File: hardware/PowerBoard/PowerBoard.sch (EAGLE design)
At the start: 137 parts, among them J1 CON-HRS-DM3AT, J2 CON-ZX62R-B-5P, J3 CON-FTSH-105-01-L-DV-K, J4 CON-S2B-PH-SM4-TB, J5 CON-PJ-102A, J6 CON-71741-0002-TOP, M1 MOUNT-HOLE3.3, M2 MOUNT-HOLE3.3, M3 MOUNT-HOLE3.3, M4 MOUNT-HOLE3.3, M5 FIDUCIAL1X2, M6 FIDUCIAL1X2, M7 FIDUCIAL1X2, M8 FIDUCIAL1X2, Q1 SI2323CDS, Q2 SI2312CDS, Q3 SI2333CDS, Q4 SI2333CDS, SW1 SWITCH-SPST, SW2 SWITCH-MS12ASG30, U1 LTC4361-2DC, U10 MAX9938FEUK, U11 MAX9938FEUK, U12 MAX9938FEUK, U13 STM32F10XCXT6, U14 LTC2942-1, U15 USBLC6-2, U2 LTC4085, U3 XC6220B331MR-G, U4 XC6220B331MR-G, U5 XC9236A15DMR-G, U6 MIC94043, U7 MAX9938FEUK, U8 MAX9938FEUK, U9 MAX9938FEUK, X1 ECX-2236, X2 ECX-31B

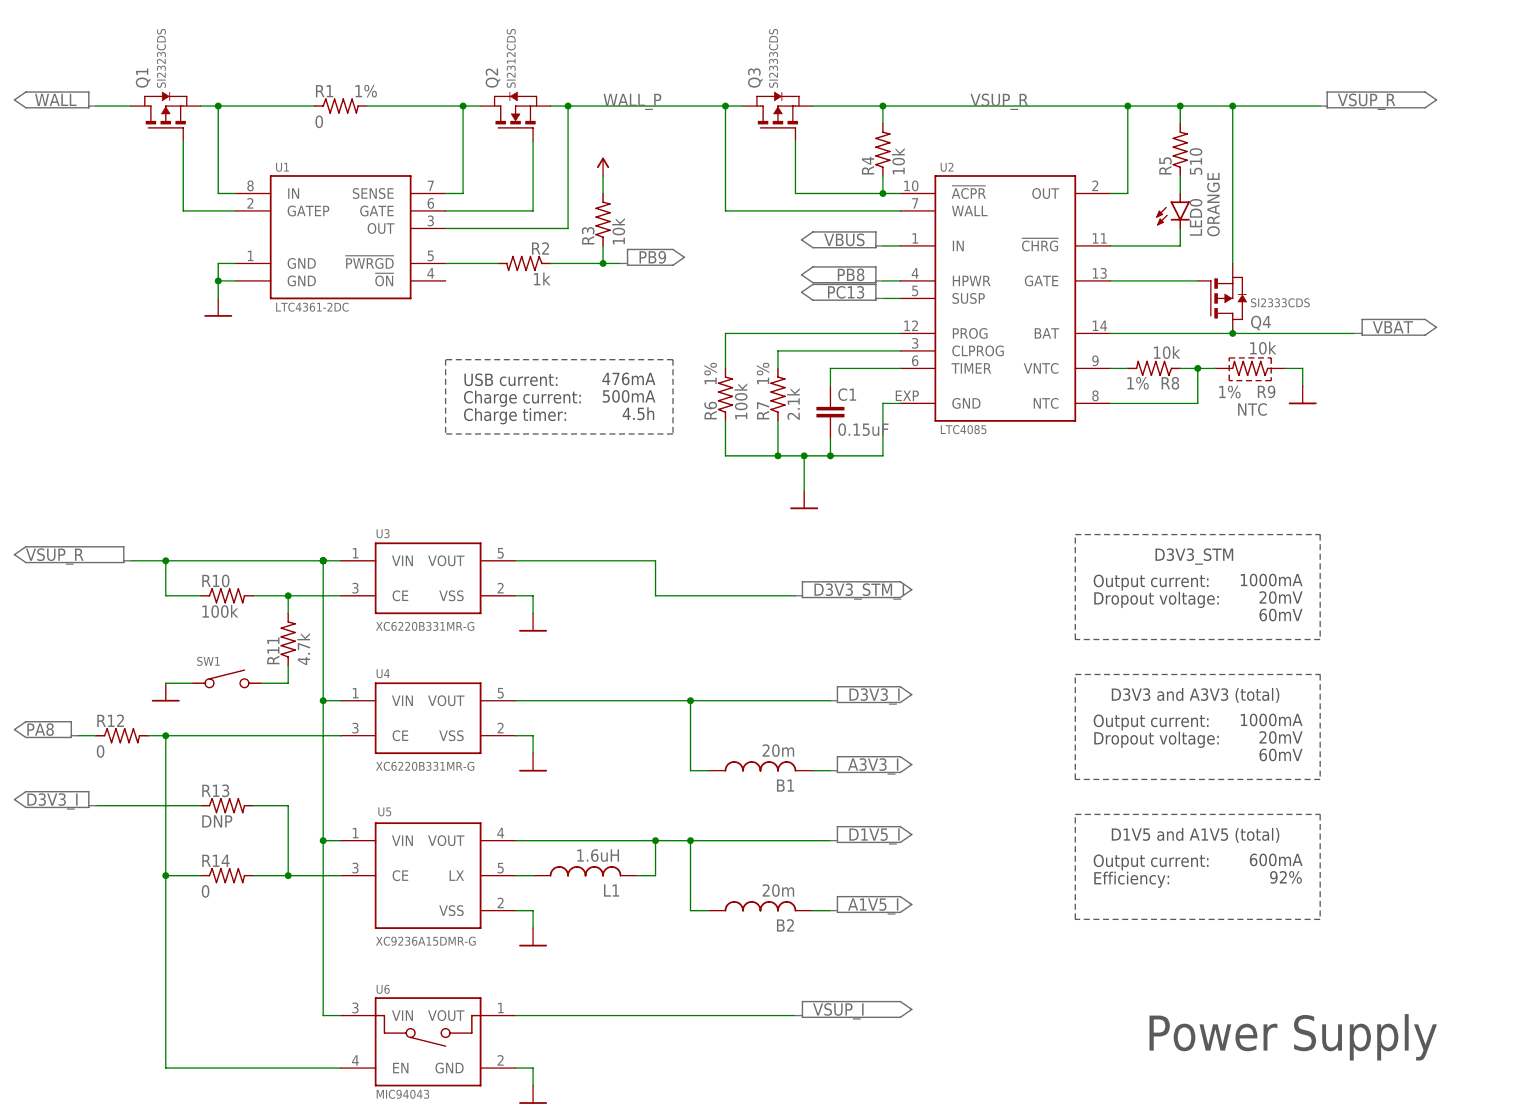
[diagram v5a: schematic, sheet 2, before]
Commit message: - Supply voltage measurement changes - PB9 monitors /CHRG (no led)
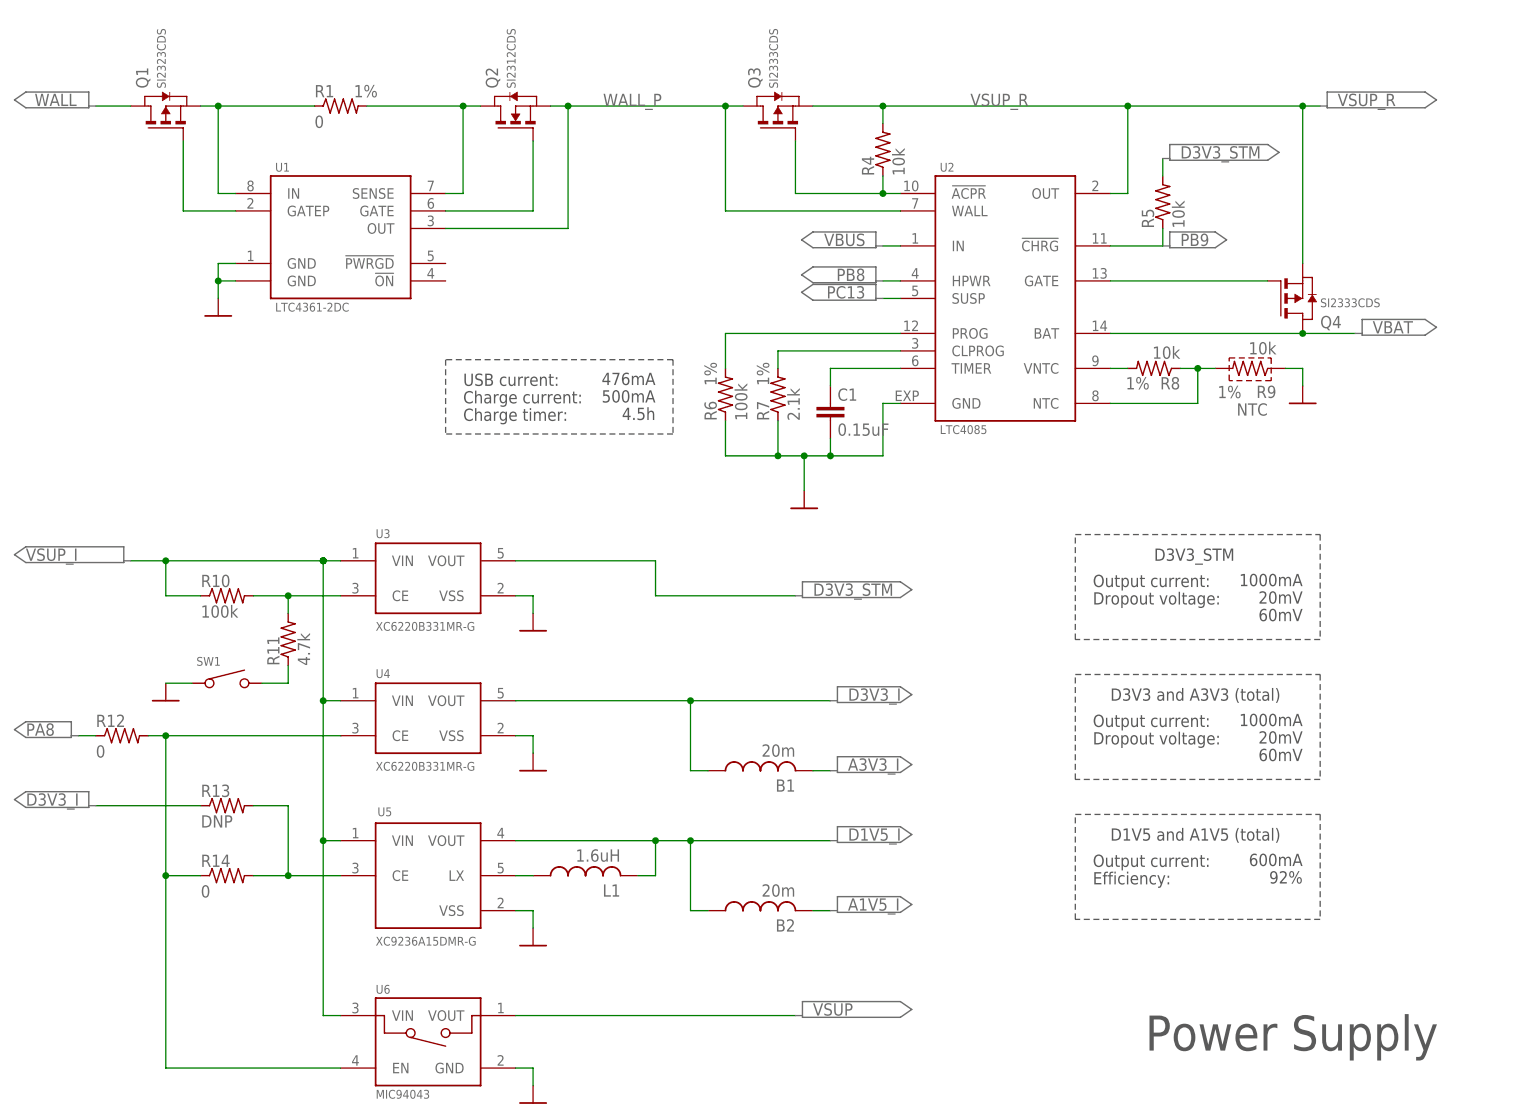
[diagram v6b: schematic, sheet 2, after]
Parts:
- removed LED0: ORANGE, powerboard:LED-ECK-3010
- removed R3: 10k, powerboard:R0603
- removed U7: MAX9938FEUK, powerboard:MAX9938FEUK
- R15: value 50m -> 100k
- R2: value 1k -> 100k; TOLERANCE (none) -> 1%
- R5: value 510 -> 10k
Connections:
- removed net !CHRG: LED0.C, U2.!CHRG
- removed net !PWRGD: R2.2, U1.!PWRGD
- removed net D3V3_STM_I: C10.1, R15.1, U3.VOUT, U7.RS+
- removed net D3V3_STM_SENSE: U13-PORTB_L.PB1, U7.OUT
- removed net N$8: LED0.A, R5.1
- removed net VSUP_SENSE: U13-PORTA_L.PA0, U8.OUT
- new net VSUP_I_SENSE: U13-PORTB_L.PB0, U8.OUT
- new net VSUP_V_SENSE: R15.1, R2.2, U13-PORTB_L.PB1
- net A1V5_SENSE: now also U13-PORTA_L.PA2; no longer U13-PORTA_L.PA3
- net A3V3_SENSE: now also U13-PORTA_L.PA3; no longer U13-PORTB_L.PB0
- net AGND: now also R2.1; no longer U7.GND, U7.GND@1
- net D1V5_SENSE: now also U13-PORTA_L.PA1; no longer U13-PORTA_L.PA2
- net D3V3_SENSE: now also U13-PORTA_L.PA0; no longer U13-PORTA_L.PA1
- net D3V3_STM: now also C10.1, R5.2, U3.VOUT; no longer R15.2, R3.2, U7.RS-
- net PB9: now also R5.1, U2.!CHRG; no longer R2.1, R3.1
- net VSUP: now also U6.VOUT; no longer R16.2, U8.RS-
- net VSUP_I: now also C11.1, C13.1, C9.1, R10.1, R16.2, U3.VIN, U4.VIN, U5.VIN, U6.VIN, U8.RS-; no longer R16.1, U6.VOUT, U8.RS+
- net VSUP_R: now also R15.2, R16.1, U8.RS+; no longer C11.1, C13.1, C9.1, R10.1, R5.2, U3.VIN, U4.VIN, U5.VIN, U6.VIN
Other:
- moved on the sheet: Q4, R15, R5

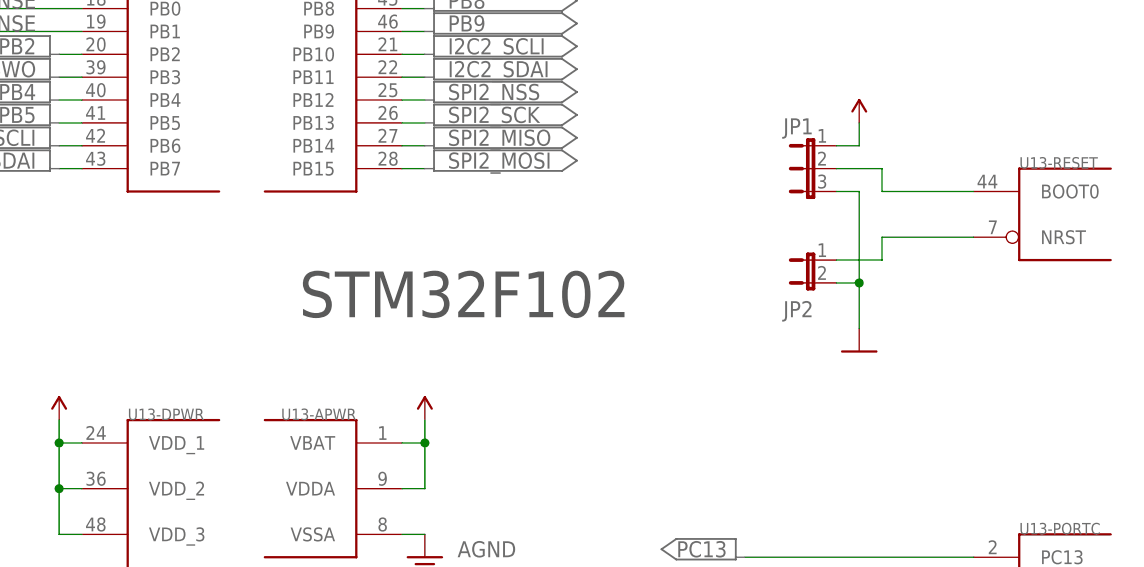
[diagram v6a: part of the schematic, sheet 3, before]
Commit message: - Pushbutton added for reset
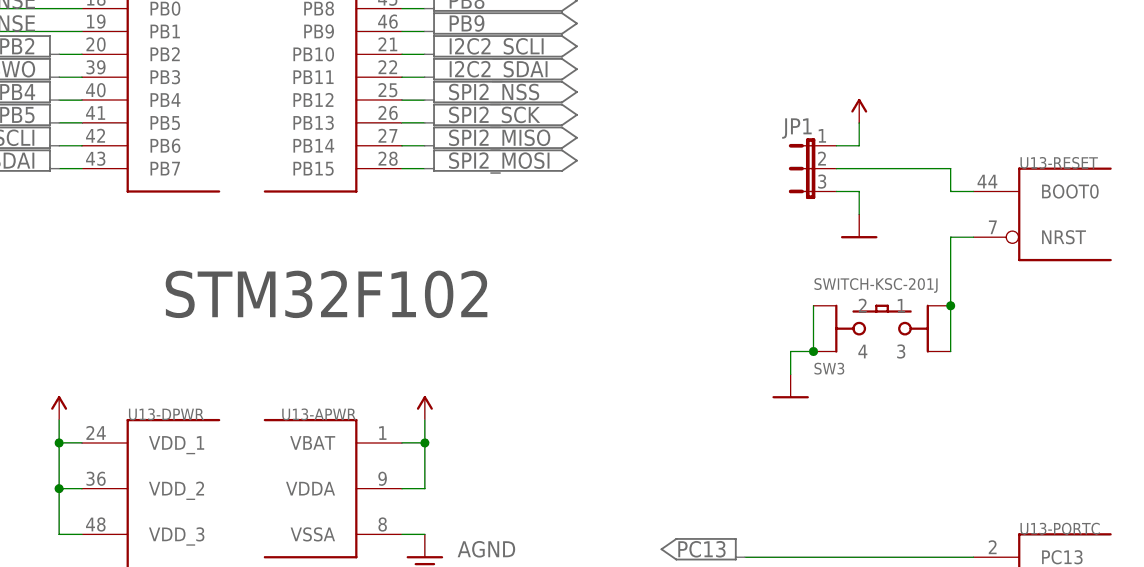
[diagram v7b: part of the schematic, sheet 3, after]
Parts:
- removed JP2: JUMPER-2PTH-LOCK, powerboard:JUMPER-2PTH-LOCK
- added SW3: SWITCH-KSC-201J, powerboard:SWITCH-KSC-201J
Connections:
- net DGND: now also SW3.2, SW3.4; no longer JP2.2
- net NRST: now also SW3.1, SW3.3; no longer JP2.1
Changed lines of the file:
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@@
 <part name="PORT58" library="powerboard" deviceset="PORT3" device=""/>
 <part name="PORT59" library="powerboard" deviceset="PORT3" device=""/>
-<part name="JP2" library="powerboard" deviceset="JUMPER-2" device="PTH-LOCK"/>
 <part name="U$37" library="powerboard" deviceset="DGND" device=""/>
 <part name="PORT60" library="powerboard" deviceset="PORT5" device=""/>
@@
 </part>
 <part name="PORT18" library="powerboard" deviceset="PORT7" device=""/>
+<part name="SW3" library="powerboard" deviceset="SWITCH-KSC" device="J" technology="-201"/>
+<part name="U$15" library="powerboard" deviceset="DGND" device=""/>
 </parts>
 <sheets>
@@
 <wire x1="89.408" y1="16.002" x2="89.408" y2="10.922" width="0.1524" layer="97" style="shortdash"/>
 <text x="182.88" y="20.32" size="5.08" layer="97">&gt;PAGE3</text>
-<text x="140.97" y="100.33" size="5.08" layer="97">STM32F102</text>
+<text x="125.73" y="100.33" size="5.08" layer="97">STM32F102</text>
 <text x="166.37" y="57.15" size="1.778" layer="97">16 MHz</text>
 <text x="91.44" y="12.7" size="1.778" layer="97">I2C 1100100</text>
@@
 <instance part="PORT58" gate="G$1" x="182.88" y="68.58" rot="MR0"/>
 <instance part="PORT59" gate="G$1" x="182.88" y="63.5" rot="MR0"/>
-<instance part="JP2" gate="A" x="198.12" y="106.68" smashed="yes" rot="MR270">
-<attribute name="NAME" x="198.12" y="100.33" size="1.778" layer="95" rot="MR0"/>
-</instance>
-<instance part="U$37" gate="G$1" x="203.2" y="96.52" rot="MR0"/>
+<instance part="U$37" gate="G$1" x="203.2" y="109.22" rot="MR0"/>
 <instance part="PORT60" gate="G$1" x="228.6" y="147.32"/>
 <instance part="PORT61" gate="G$1" x="91.44" y="17.78" rot="MR0"/>
@@
 </instance>
 <instance part="PORT18" gate="G$1" x="10.16" y="177.8" rot="MR0"/>
+<instance part="SW3" gate="G$1" x="205.74" y="99.06"/>
+<instance part="U$15" gate="G$1" x="195.58" y="91.44" rot="MR0"/>
 </instances>
 <busses>
@@
 </segment>
 <segment>
-<wire x1="203.2" y1="99.06" x2="203.2" y2="104.14" width="0.1524" layer="91"/>
-<wire x1="203.2" y1="104.14" x2="200.66" y2="104.14" width="0.1524" layer="91"/>
-<wire x1="200.66" y1="114.3" x2="203.2" y2="114.3" width="0.1524" layer="91"/>
-<wire x1="203.2" y1="114.3" x2="203.2" y2="104.14" width="0.1524" layer="91"/>
-<junction x="203.2" y="104.14"/>
-<pinref part="U$37" gate="G$1" pin="DGND"/>
-<pinref part="JP2" gate="A" pin="2"/>
-<pinref part="JP1" gate="G$1" pin="3"/>
-</segment>
-<segment>
 <wire x1="144.78" y1="17.78" x2="144.78" y2="15.24" width="0.1524" layer="91"/>
 <wire x1="142.24" y1="17.78" x2="144.78" y2="17.78" width="0.1524" layer="91"/>
 <pinref part="U$2" gate="G$1" pin="DGND"/>
 <pinref part="U14" gate="LTC3677-2" pin="GND"/>
+</segment>
+<segment>
+<wire x1="200.66" y1="114.3" x2="203.2" y2="114.3" width="0.1524" layer="91"/>
+<pinref part="JP1" gate="G$1" pin="3"/>
+<pinref part="U$37" gate="G$1" pin="DGND"/>
+<wire x1="203.2" y1="114.3" x2="203.2" y2="111.76" width="0.1524" layer="91"/>
+</segment>
+<segment>
+<pinref part="SW3" gate="G$1" pin="2"/>
+<pinref part="SW3" gate="G$1" pin="4"/>
+<junction x="198.12" y="96.52"/>
+<wire x1="198.12" y1="101.6" x2="198.12" y2="96.52" width="0.1524" layer="91"/>
+<wire x1="198.12" y1="96.52" x2="195.58" y2="96.52" width="0.1524" layer="91"/>
+<pinref part="U$15" gate="G$1" pin="DGND"/>
+<wire x1="195.58" y1="96.52" x2="195.58" y2="93.98" width="0.1524" layer="91"/>
 </segment>
 </net>
@@
 <net name="NRST" class="0">
 <segment>
-<wire x1="215.9" y1="109.22" x2="205.74" y2="109.22" width="0.1524" layer="91"/>
-<wire x1="205.74" y1="109.22" x2="205.74" y2="106.68" width="0.1524" layer="91"/>
-<wire x1="205.74" y1="106.68" x2="200.66" y2="106.68" width="0.1524" layer="91"/>
+<wire x1="215.9" y1="109.22" x2="213.36" y2="109.22" width="0.1524" layer="91"/>
+<wire x1="213.36" y1="109.22" x2="213.36" y2="101.6" width="0.1524" layer="91"/>
 <pinref part="U13" gate="-RESET" pin="NRST"/>
-<pinref part="JP2" gate="A" pin="1"/>
+<pinref part="SW3" gate="G$1" pin="1"/>
+<wire x1="213.36" y1="101.6" x2="213.36" y2="96.52" width="0.1524" layer="91"/>
+<junction x="213.36" y="101.6"/>
+<pinref part="SW3" gate="G$1" pin="3"/>
 </segment>
 </net>
@@
 <net name="BOOT0" class="0">
 <segment>
-<wire x1="215.9" y1="114.3" x2="205.74" y2="114.3" width="0.1524" layer="91"/>
-<wire x1="205.74" y1="114.3" x2="205.74" y2="116.84" width="0.1524" layer="91"/>
-<wire x1="205.74" y1="116.84" x2="200.66" y2="116.84" width="0.1524" layer="91"/>
+<wire x1="215.9" y1="114.3" x2="213.36" y2="114.3" width="0.1524" layer="91"/>
+<wire x1="213.36" y1="114.3" x2="213.36" y2="116.84" width="0.1524" layer="91"/>
+<wire x1="213.36" y1="116.84" x2="200.66" y2="116.84" width="0.1524" layer="91"/>
 <pinref part="U13" gate="-RESET" pin="BOOT0"/>
 <pinref part="JP1" gate="G$1" pin="2"/>
